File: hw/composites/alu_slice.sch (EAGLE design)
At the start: 13 parts, among them CON2 GENERIC-2X10

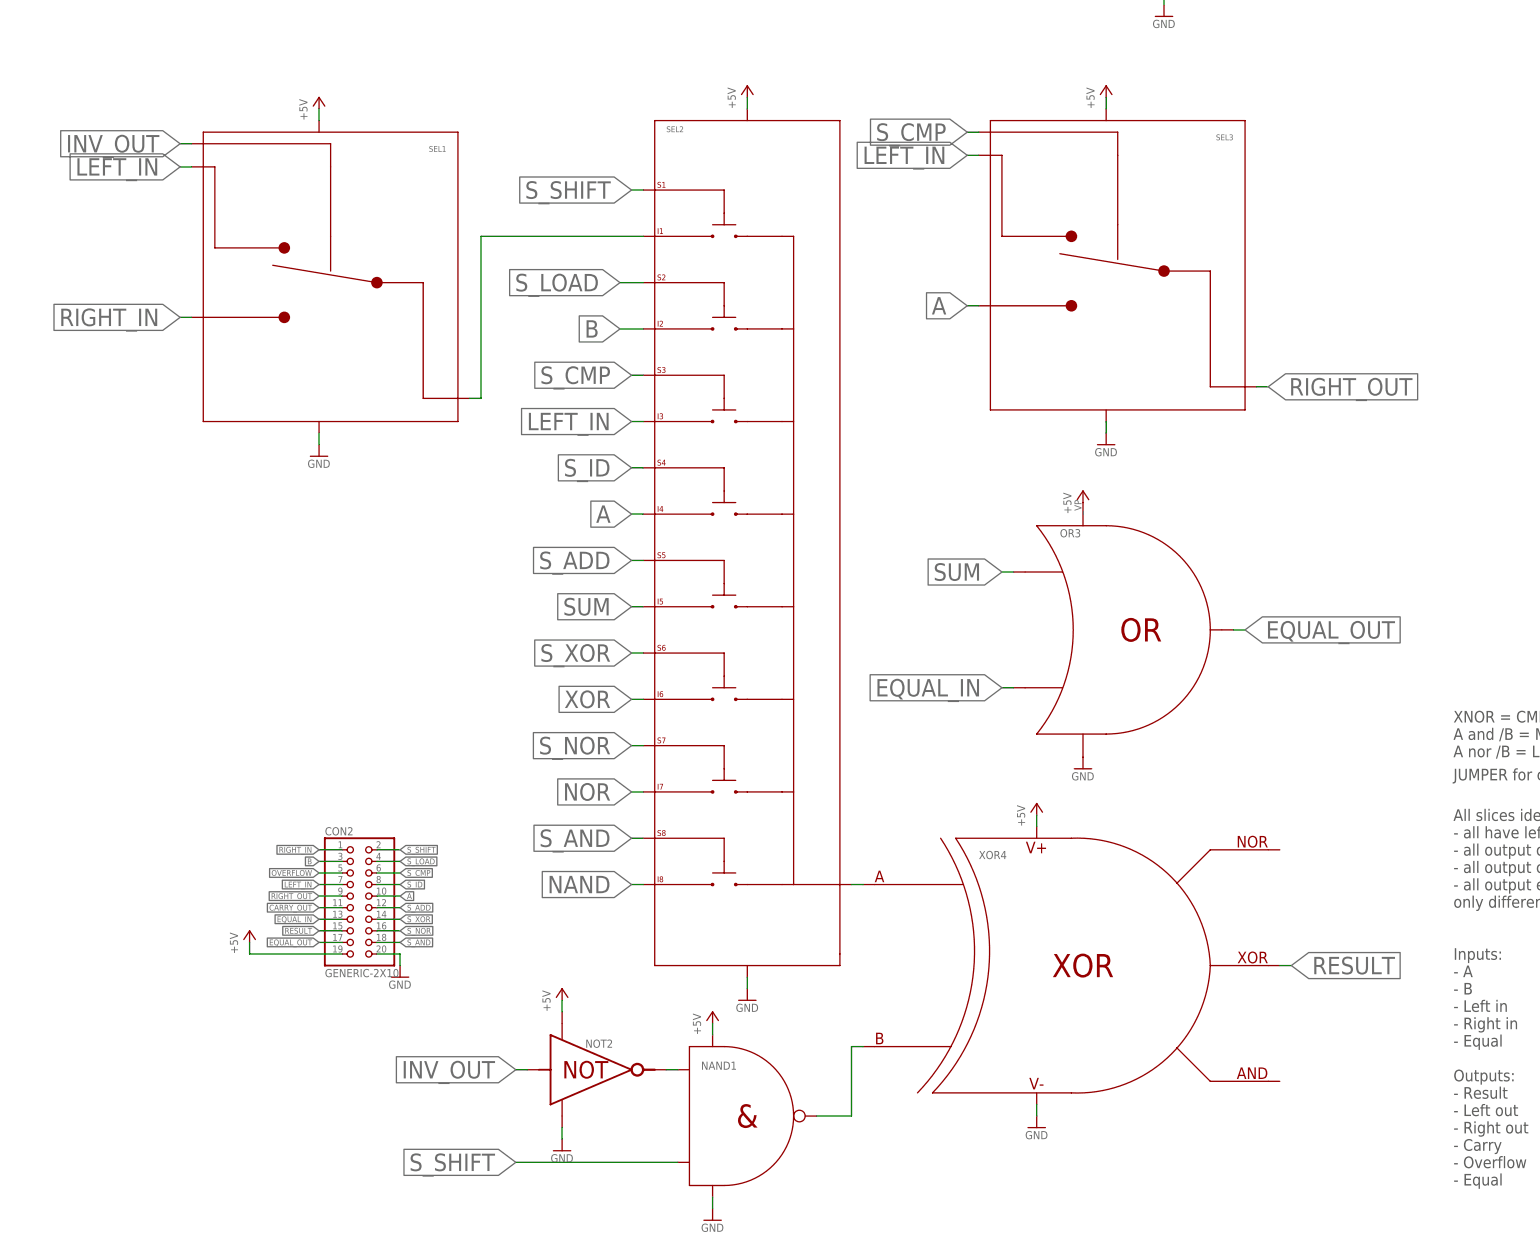
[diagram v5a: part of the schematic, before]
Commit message: Adds first orgaized integration tests
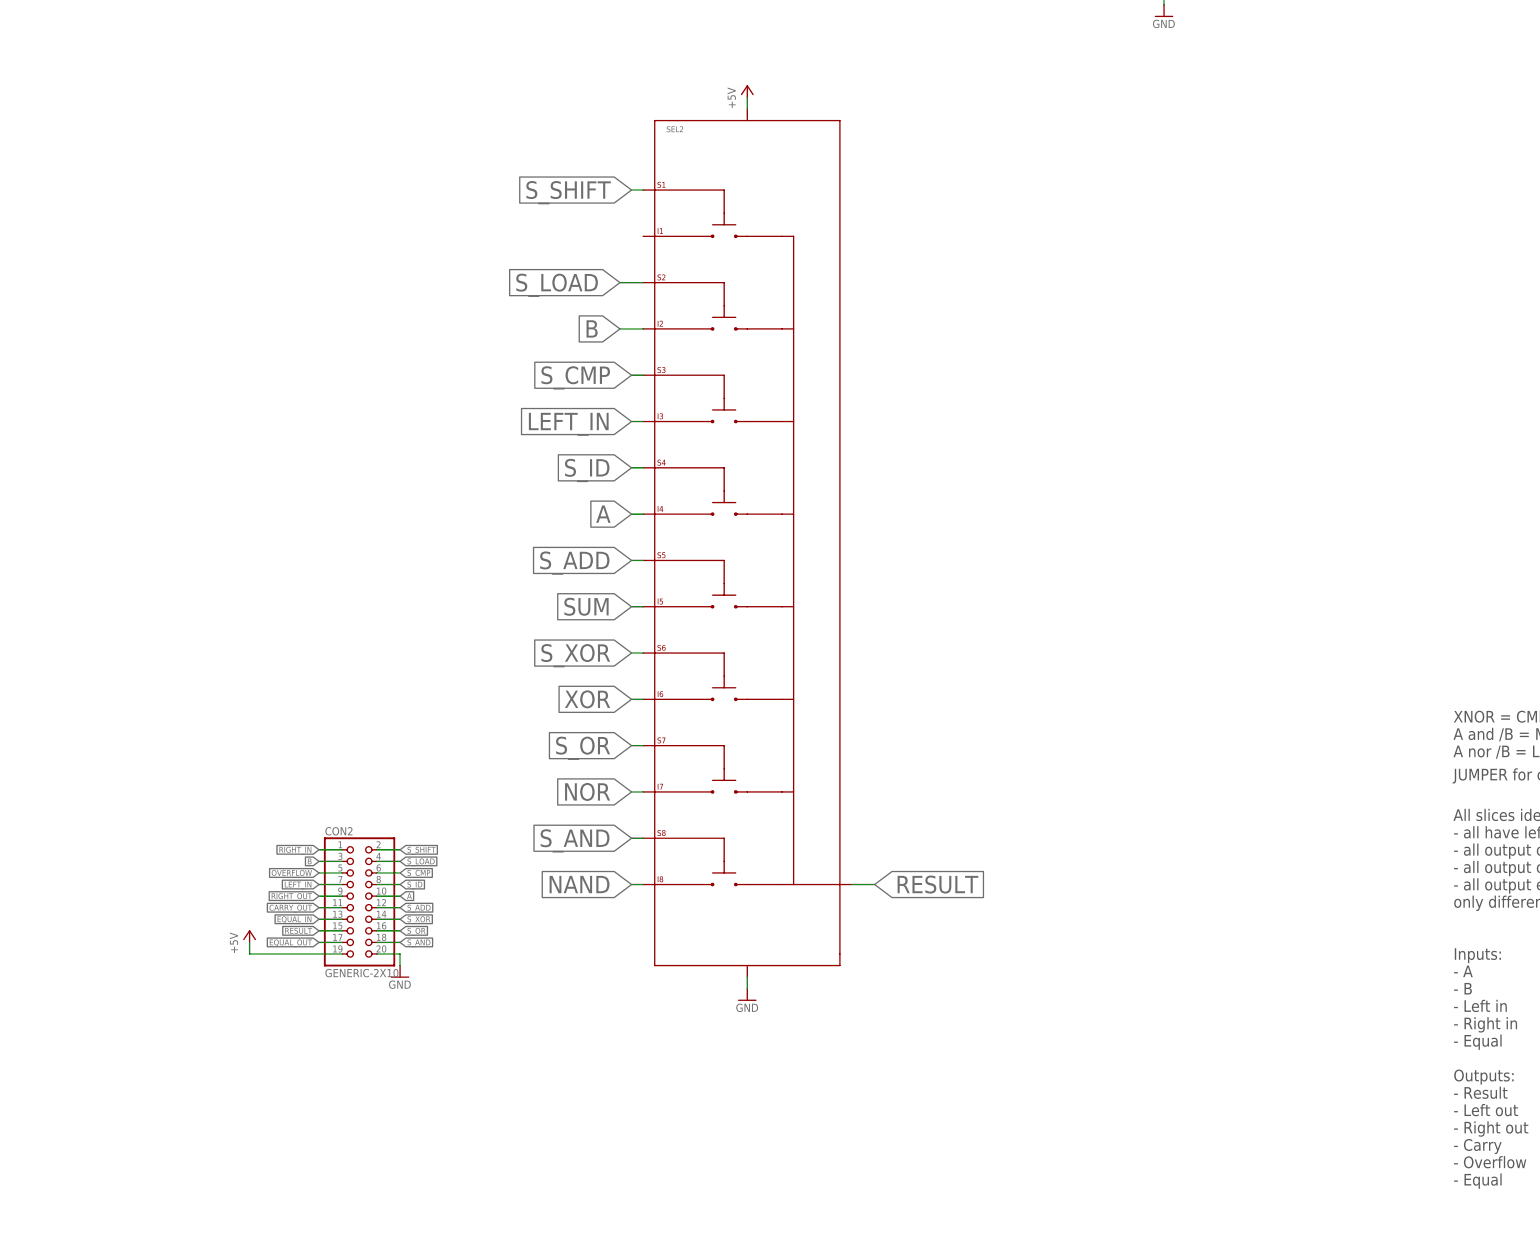
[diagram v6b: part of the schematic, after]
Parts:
- removed NAND1: NAND, p.peter-gator:NAND
- removed NOT2: NOTVERTICAL, p.peter-gator:NOTVERTICAL
- removed OR3: OR, p.peter-gator:OR
- removed SEL1, SEL3: 1_BIT_SELECT, p.peter-gator:1_BIT_SELECT
- removed XOR4: XOR, p.peter-gator:XOR
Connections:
- net S_NOR renamed S_OR
- removed net INV_OUT: NOT2.A, SEL1.SEL
- removed net N$1: NAND1.NAND, XOR4.B
- removed net N$2: SEL1.OUT, SEL2.I1
- removed net N$3: SEL2.OUT, XOR4.A
- removed net N$7: NAND1.A, NOT2.NOT
- net +5V: no longer NAND1._VP, NOT2._VP, OR3._VP, SEL1._VP, SEL3._VP, XOR4._VP
- net A: no longer SEL3.B
- net EQUAL_IN: no longer OR3.B
- net EQUAL_OUT: no longer OR3.OR
- net GND: no longer NAND1._VN, NOT2._VN, OR3._VN, SEL1._VN, SEL3._VN, XOR4._VN
- net LEFT_IN: no longer SEL1.A, SEL3.A
- net RESULT: now also SEL2.OUT; no longer XOR4.XOR
- net RIGHT_IN: no longer SEL1.B
- net RIGHT_OUT: no longer SEL3.OUT
- net SUM: no longer OR3.A
- net S_CMP: no longer SEL3.SEL
- net S_SHIFT: no longer NAND1.B

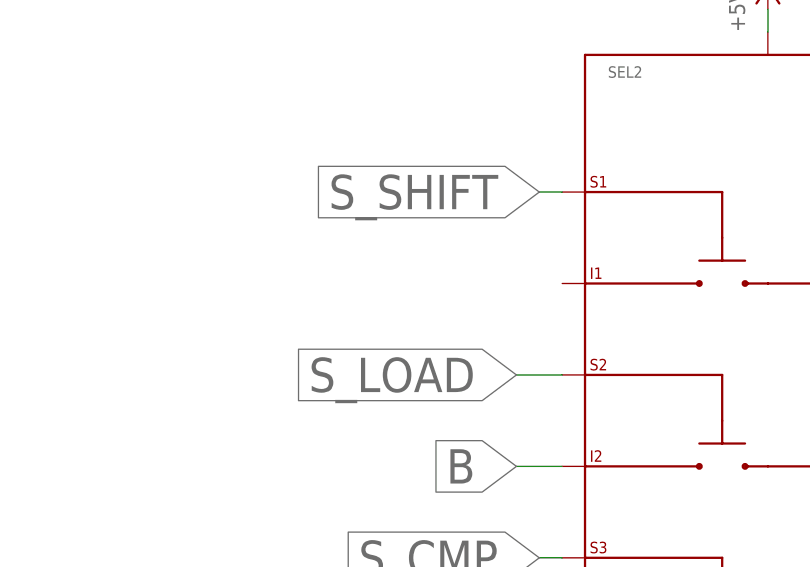
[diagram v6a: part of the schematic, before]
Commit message: fixes some offset and juction issues
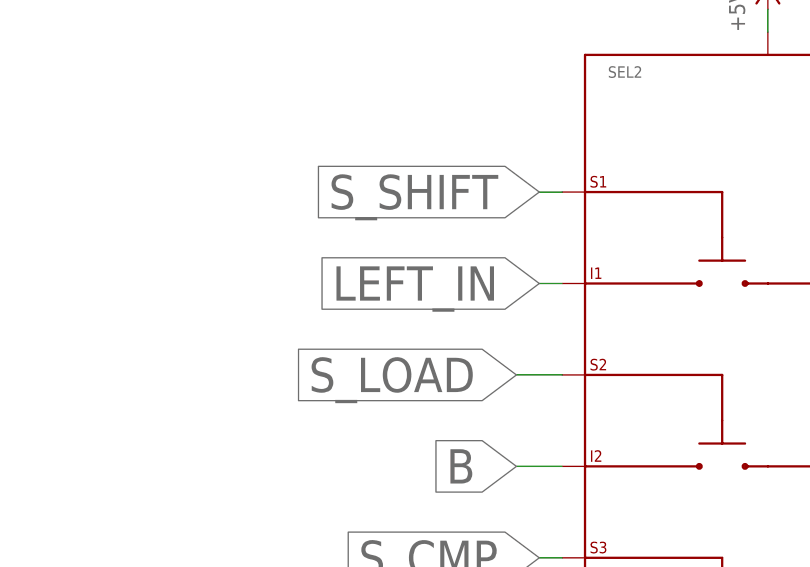
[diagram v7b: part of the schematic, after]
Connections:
- net LEFT_IN: now also SEL2.I1
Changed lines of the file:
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@@
 <label x="-27.94" y="-25.4" size="1.27" layer="95" ratio="9" rot="R180" xref="yes"/>
+</segment>
+<segment>
+<pinref part="SEL2" gate="G$1" pin="I1"/>
+<wire x1="43.18" y1="116.84" x2="40.64" y2="116.84" width="0.1524" layer="91"/>
+<label x="40.64" y="116.84" size="3.81" layer="95" ratio="12" rot="R180" xref="yes"/>
 </segment>
 </net>
@@
 </sheet>
 </sheets>
+<errors>
+</errors>
 </schematic>
 </drawing>
